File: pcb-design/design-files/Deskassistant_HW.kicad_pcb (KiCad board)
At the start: 4 copper layers, 183.5 x 108 mm, 127 parts, among them J1 USB_C_Receptacle_USB2.0_16P, J2 Conn_01x06_Socket, J3 62684-502100ALF, J4 USB_A, J5 ComputeModule5-CM5_UnitA, J6 ComputeModule5-CM5_UnitB, Q1 1AM, SW1 SW_Push, SW2 SW_Push, SW3 SW_Push, SW4 SW_Push, SW5 SW_Push, U1 TPS62162DSG, U2 TPS259472LRPWR, U3 TFP401APZPR, U4 TPS61165DBV, U5 TPS61040DBV, U6 TPS2041CDBV

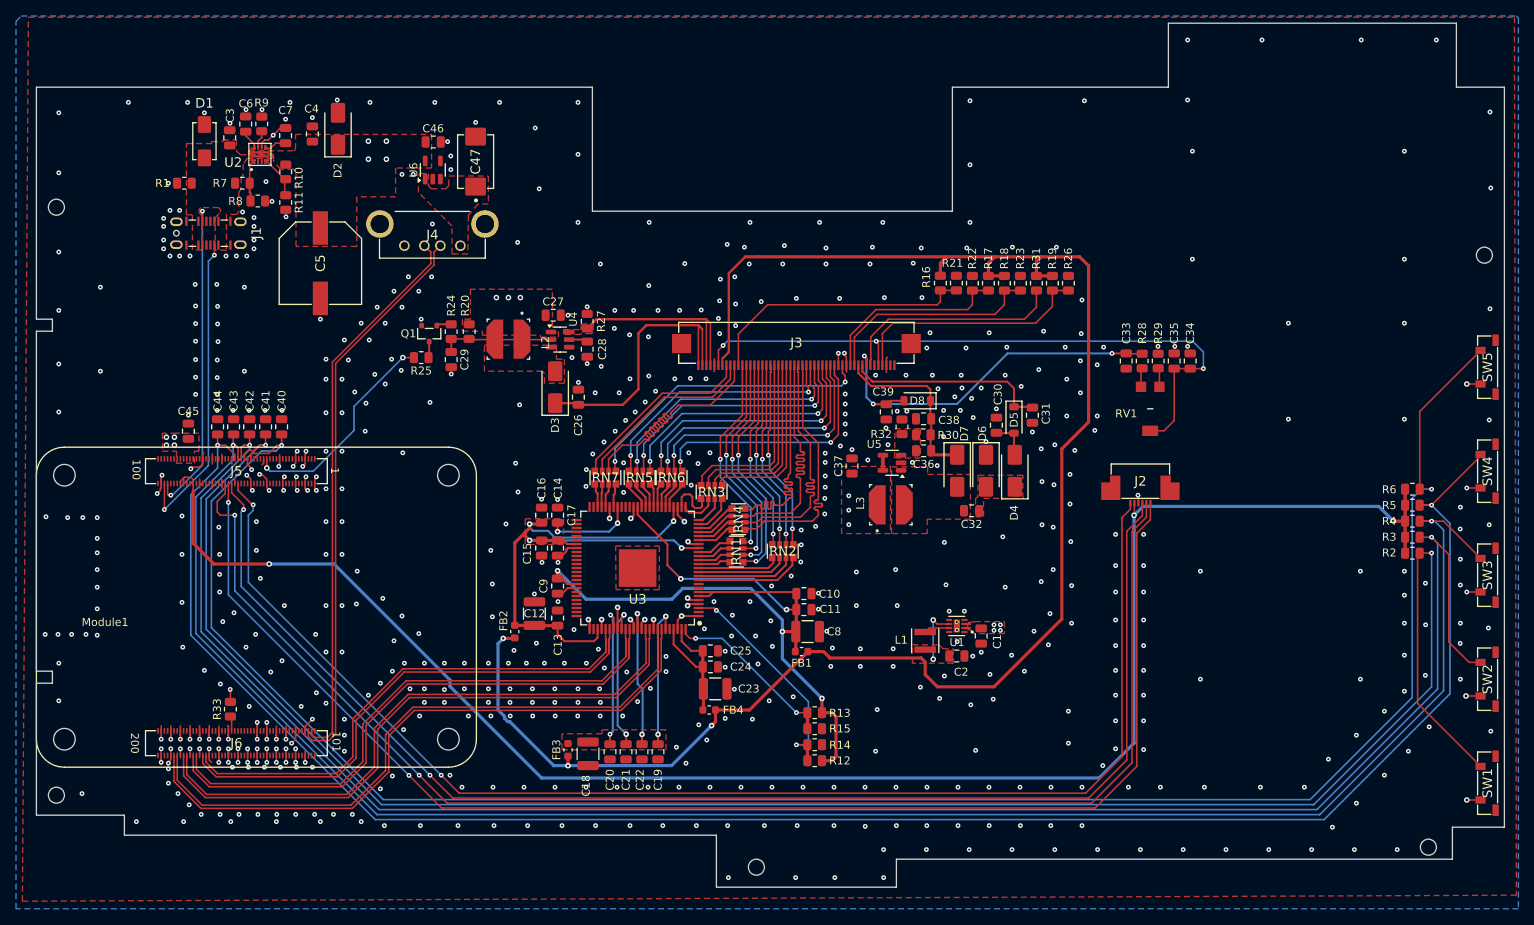
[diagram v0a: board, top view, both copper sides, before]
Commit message: Fix HW rev B issues
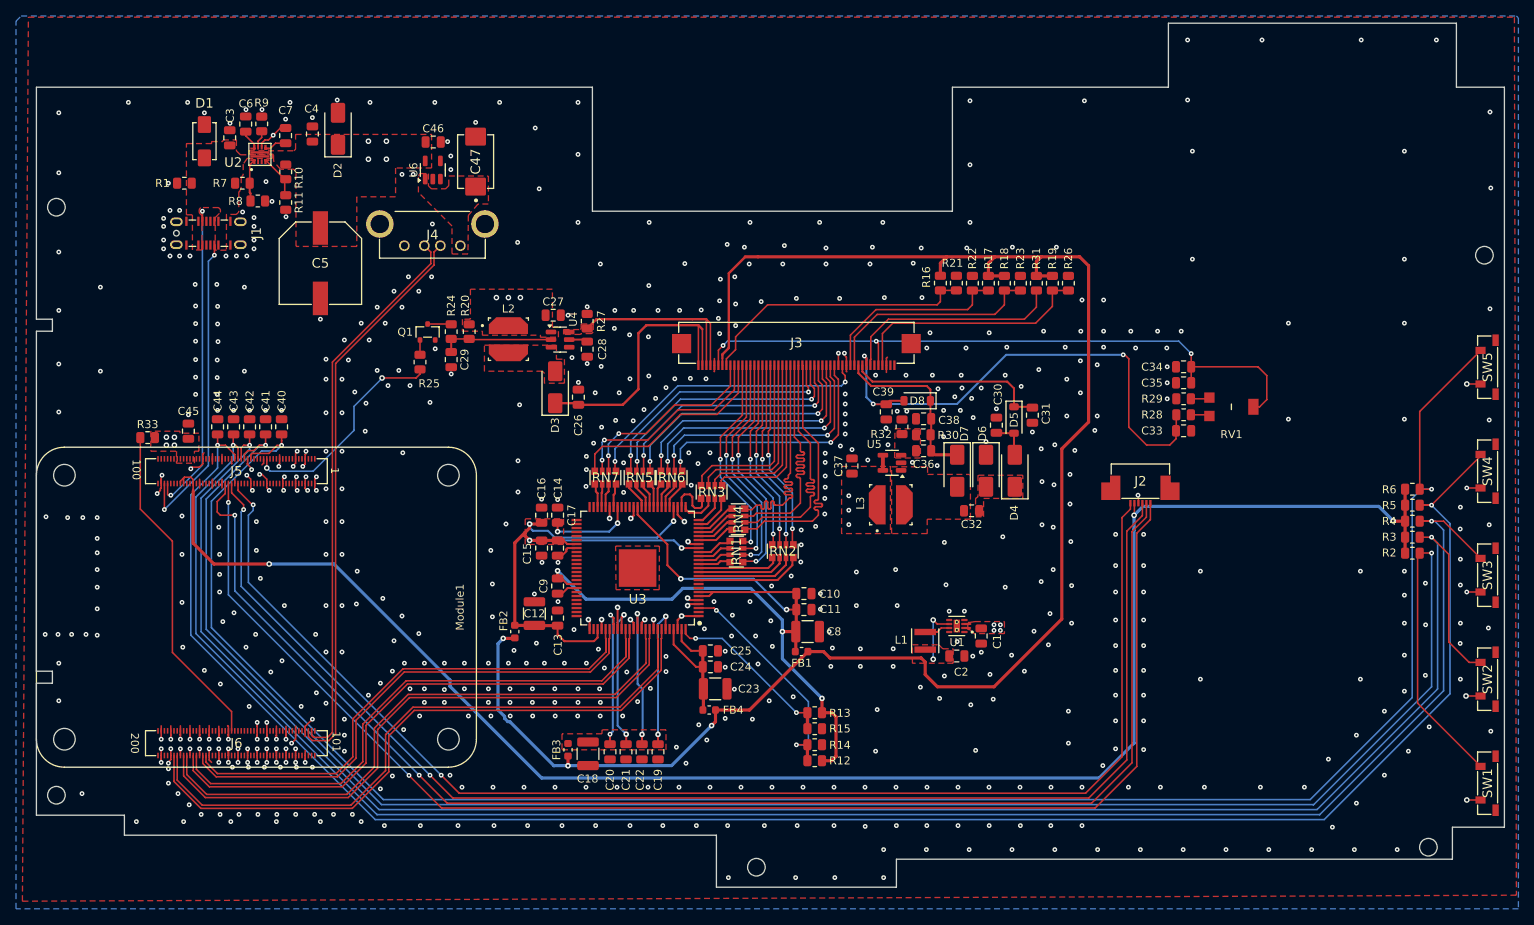
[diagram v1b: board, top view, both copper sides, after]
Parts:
- removed the REF** at (146.0, 144.5)
- removed the REF** at (58.5, 135.5)
- removed the REF** at (230.0, 142.0)
- removed the REF** at (237.0, 68.0)
- removed the REF** at (58.5, 62.0)
- added REF**: MountingHole_2.2mm, Deskassistant_HW:MountingHole_2.2mm, F.Cu at (58.5, 135.5)
- added REF**: MountingHole_2.2mm, Deskassistant_HW:MountingHole_2.2mm, F.Cu at (237.0, 68.0)
- added REF**: MountingHole_2.2mm, Deskassistant_HW:MountingHole_2.2mm, F.Cu at (58.5, 62.0)
- added REF**: MountingHole_2.2mm, Deskassistant_HW:MountingHole_2.2mm, F.Cu at (146.0, 144.5)
- added REF**: MountingHole_2.2mm, Deskassistant_HW:MountingHole_2.2mm, F.Cu at (230.0, 142.0)
- D5: value D_Zener -> 5.6V
- D8: value D_Zener -> 9.1
- moved R33 35.5 mm to (69.9, 90.8), turned to 0 degrees
- moved C33 11.3 mm to (199.4, 90.0), turned to 0 degrees
- moved RV1 10.2 mm to (205.4, 87.0), turned to -90 degrees
- moved R28 8.49 mm to (199.4, 88.0), turned to 0 degrees
- moved R29 5.69 mm to (199.4, 86.0), turned to 180 degrees
- moved C35 2.97 mm to (199.4, 84.0), turned to 180 degrees
- moved C34 1.10 mm to (199.4, 82.0), turned to 180 degrees
- moved R25 0.58 mm to (104.0, 81.4), turned to 90 degrees
- moved Q1 0.28 mm to (104.9, 77.6), turned to 0 degrees
- turned L2 to 0 degrees
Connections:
- net Net-(J3-Pad7) renamed /display connection/RST
- J3 pad 40: /display connection/MODE -> Net-(J3-HS)
- J3 pad 41: Net-(RN7C-R3.2) -> Net-(J3-VS)
- J3 pad 42: Net-(RN7B-R2.2) -> Net-(J3-DE)
- J3 pad 43: Net-(RN7A-R1.2) -> /display connection/MODE
- R24 pad 2: Net-(Q1-B) -> Net-(Q1-C)
- R25 pad 1: Net-(Q1-C) -> /CM5/BK_CTRL
- R25 pad 2: /CM5/BK_CTRL -> Net-(Q1-B)
- RN7 pad 6: Net-(RN7C-R3.2) -> Net-(J3-DE)
- RN7 pad 7: Net-(RN7B-R2.2) -> Net-(J3-VS)
- RN7 pad 8: Net-(RN7A-R1.2) -> Net-(J3-HS)
- SW1 pad : GND -> (no net)
- SW2 pad : GND -> (no net)
- SW3 pad : GND -> (no net)
- SW4 pad : GND -> (no net)
- SW5 pad : GND -> (no net)
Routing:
- net Net-(J6-HDMI0_HOTPLUG): track 1.86 -> 41.4 mm
- net Net-(RN7C-R3.2): track 32.4 -> 0.00 mm
- net Net-(J3-HS): track 0.00 -> 26.7 mm
- net Net-(J3-VS): track 0.00 -> 26.0 mm, vias 0 -> 2
- net Net-(J3-DE): track 0.00 -> 24.3 mm, vias 0 -> 2
- net Net-(RN7A-R1.2): track 23.4 -> 0.00 mm
- net Net-(RN7B-R2.2): track 23.3 -> 0.00 mm
- net /display connection/AVDD: track 48.0 -> 65.2 mm
- net +5V: track 4.95 -> 3.38 mm, vias 19 -> 18
- net /display connection/VCOM: track 82.4 -> 83.8 mm
- net Net-(Q1-C): track 2.10 -> 2.96 mm
- net /display connection/MODE: track 34.2 -> 34.8 mm
- net /CM5/BK_CTRL: track 27.3 -> 27.8 mm
- net GND: vias 687 -> 695

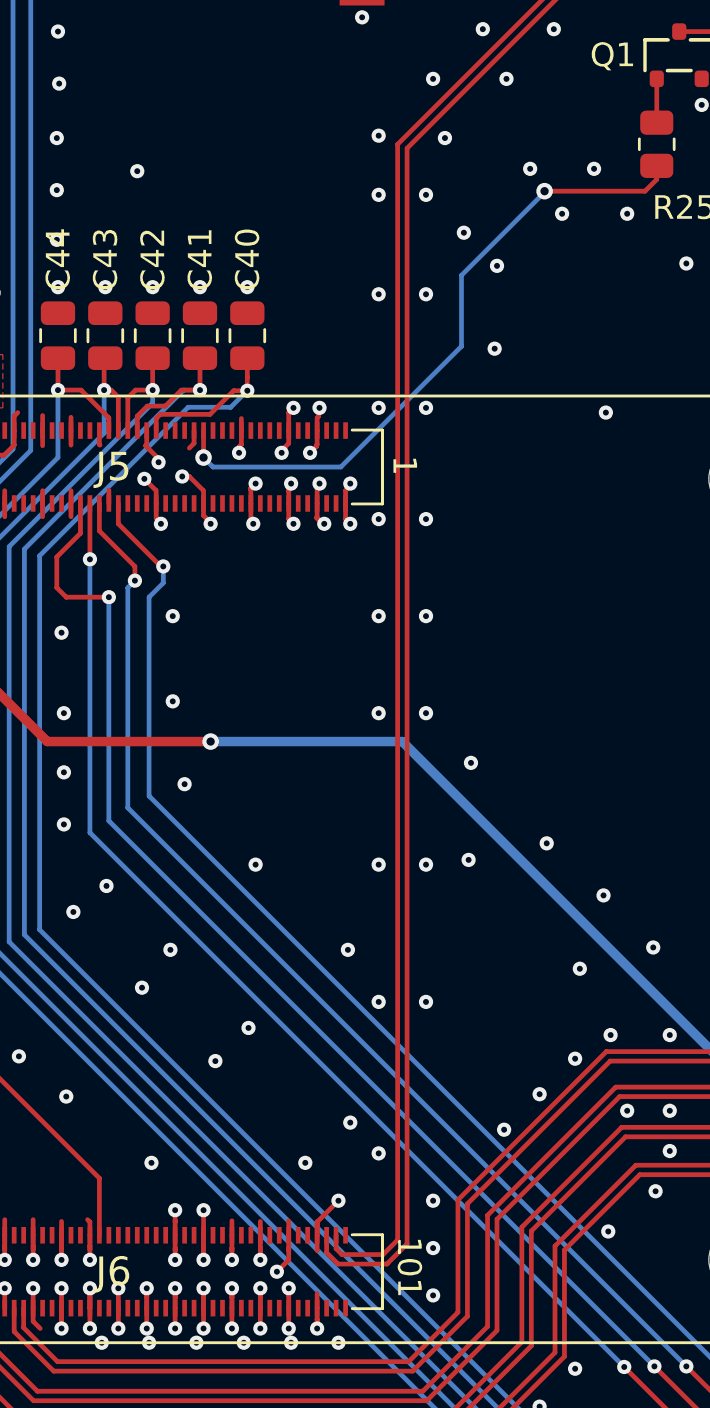
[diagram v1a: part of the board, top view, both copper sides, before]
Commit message: Fix USB D+ and D- connections
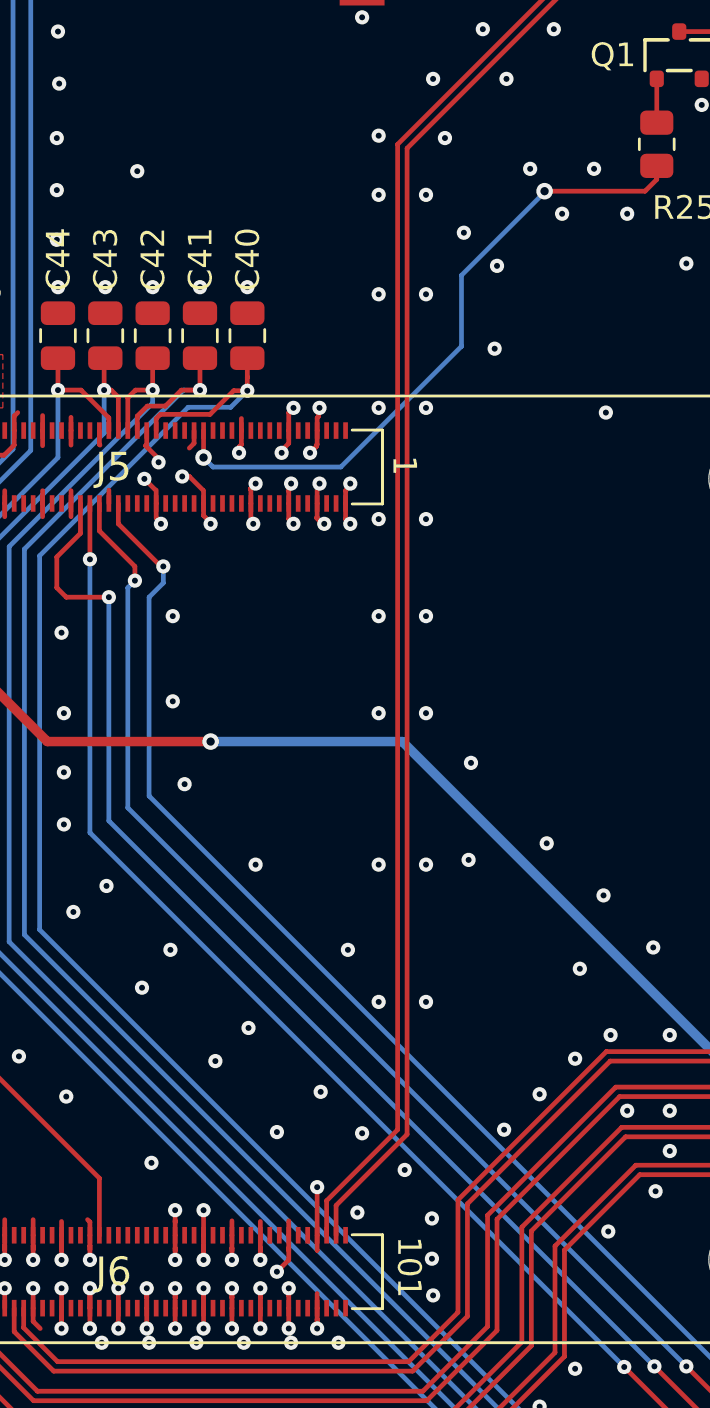
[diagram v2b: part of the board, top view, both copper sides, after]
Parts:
- D8: value 9.1 -> 9.1V
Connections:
- J6 pad 103: /CM5/USB+ -> /CM5/USB-
- J6 pad 105: /CM5/USB- -> /CM5/USB+
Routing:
- net /CM5/USB-: track 71.1 -> 67.3 mm
- net /CM5/USB+: track 69.8 -> 67.3 mm
- net GND: vias 695 -> 697
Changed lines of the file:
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@@
 			(size 0.2 0.7)
 			(layers "F.Cu" "F.Mask" "F.Paste")
-			(net 59 "/CM5/USB+")
+			(net 58 "/CM5/USB-")
 			(pinfunction "USB2_N")
 			(pintype "passive")
@@
 			(size 0.2 0.7)
 			(layers "F.Cu" "F.Mask" "F.Paste")
-			(net 58 "/CM5/USB-")
+			(net 59 "/CM5/USB+")
 			(pinfunction "USB2_P")
 			(pintype "passive")
@@
 			)
 		)
-		(property "Value" "9.1"
+		(property "Value" "9.1V"
 			(at 0 2.1 0)
 			(layer "F.Fab")
@@
 	)
 	(segment
-		(start 89.6 127.46)
-		(end 89.6 127.1)
-		(width 0.2)
-		(layer "F.Cu")
-		(net 1)
-	)
-	(segment
 		(start 86.3 94.15)
 		(end 86.4 94.05)
@@
 	)
 	(segment
-		(start 89.6 127.1)
-		(end 89.6 126.9)
-		(width 0.2)
-		(layer "F.Cu")
-		(net 1)
-	)
-	(segment
 		(start 75.2 127.9)
 		(end 75.2 128.05)
@@
 	)
 	(segment
+		(start 89.6 127.46)
+		(end 89.6 125.42647)
+		(width 0.2)
+		(layer "F.Cu")
+		(net 1)
+	)
+	(segment
 		(start 88.4 127.46)
 		(end 88.4 126.85)
@@
 	)
 	(segment
-		(start 89.6 126.9)
-		(end 90.5 126)
-		(width 0.2)
-		(layer "F.Cu")
-		(net 1)
-	)
-	(segment
 		(start 74 127.9)
 		(end 74 128.05)
@@
 	)
 	(segment
-		(start 89.6 127.1)
-		(end 89.6 126.875)
-		(width 0.2)
-		(layer "F.Cu")
-		(net 1)
-	)
-	(segment
 		(start 80.4 94.05)
 		(end 80.425 94.075)
@@
 	)
 	(via
-		(at 91 122.7)
+		(at 91.5 123.15)
 		(size 0.6)
 		(drill 0.25)
@@
 	)
 	(via
-		(at 94.5 128)
+		(at 91.3 126.5)
 		(size 0.6)
 		(drill 0.25)
@@
 	)
 	(via
+		(at 94.45 128.45)
+		(size 0.6)
+		(drill 0.25)
+		(layers "F.Cu" "B.Cu")
+		(free yes)
+		(net 1)
+	)
+	(via
 		(at 183.5 67)
 		(size 0.6)
@@
 	)
 	(via
-		(at 92.2 124)
+		(at 89.75 121.4)
 		(size 0.6)
 		(drill 0.25)
@@
 	)
 	(via
-		(at 89.1 124.4)
+		(at 87.9 123.1)
 		(size 0.6)
 		(drill 0.25)
@@
 	)
 	(via
-		(at 94.5 126)
+		(at 93.3 124.7)
 		(size 0.6)
 		(drill 0.25)
@@
 	)
 	(via
+		(at 94.45 126.75)
+		(size 0.6)
+		(drill 0.25)
+		(layers "F.Cu" "B.Cu")
+		(free yes)
+		(net 1)
+	)
+	(via
 		(at 151.6 104.2)
 		(size 0.6)
@@
 	)
 	(via
-		(at 90.5 126)
+		(at 89.6 125.42647)
 		(size 0.6)
 		(drill 0.25)
@@
 	)
 	(segment
-		(start 92.55 128.675)
-		(end 90.484314 128.675)
+		(start 90.4 126.2)
+		(end 90.4 127.46)
 		(width 0.2)
 		(layer "F.Cu")
@@
 	(segment
 		(start 93.4 81.532844)
-		(end 93.4 127.825)
-		(width 0.2)
-		(layer "F.Cu")
-		(net 58)
-	)
-	(segment
-		(start 105.7 67.6025)
-		(end 105.7 69.232844)
-		(width 0.2)
-		(layer "F.Cu")
-		(net 58)
-	)
-	(segment
-		(start 90 128.190686)
-		(end 90 127.46)
+		(end 93.4 123.2)
 		(width 0.2)
 		(layer "F.Cu")
@@
 	)
 	(segment
-		(start 93.4 127.825)
-		(end 92.55 128.675)
+		(start 93.4 123.2)
+		(end 90.4 126.2)
 		(width 0.2)
 		(layer "F.Cu")
@@
 	)
 	(segment
-		(start 90.484314 128.675)
-		(end 90 128.190686)
+		(start 105.7 67.6025)
+		(end 105.7 69.232844)
 		(width 0.2)
 		(layer "F.Cu")
@@
 	)
 	(segment
-		(start 90.4 128.025)
-		(end 90.4 127.46)
-		(width 0.2)
-		(layer "F.Cu")
-		(net 59)
-	)
-	(segment
 		(start 104.5 66.8025)
 		(end 105.3 67.6025)
@@
 	)
 	(segment
-		(start 93 127.659314)
-		(end 92.384314 128.275)
+		(start 105.3 69.067156)
+		(end 93 81.367156)
 		(width 0.2)
 		(layer "F.Cu")
@@
 	(segment
 		(start 93 81.367156)
-		(end 93 127.659314)
-		(width 0.2)
-		(layer "F.Cu")
-		(net 59)
-	)
-	(segment
-		(start 105.3 67.6025)
-		(end 105.3 69.067156)
+		(end 93 123)
 		(width 0.2)
 		(layer "F.Cu")
@@
 	)
 	(segment
-		(start 92.384314 128.275)
-		(end 90.65 128.275)
+		(start 90 126)
+		(end 90 127.46)
 		(width 0.2)
 		(layer "F.Cu")
@@
 	)
 	(segment
-		(start 90.65 128.275)
-		(end 90.4 128.025)
+		(start 105.3 67.6025)
+		(end 105.3 69.067156)
 		(width 0.2)
 		(layer "F.Cu")
@@
 	)
 	(segment
-		(start 105.3 69.067156)
-		(end 93 81.367156)
+		(start 93 123)
+		(end 90 126)
 		(width 0.2)
 		(layer "F.Cu")
